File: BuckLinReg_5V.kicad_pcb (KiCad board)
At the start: 4 copper layers, 96 x 56 mm, 70 parts, among them J1 Barrel_Jack, J2 796638-4, J3 1x2 Male, Q1 PMBT2222, Q2 SQD40061EL, SW1 SW_SPDT, U1 TLV76050DBZT, U2 LMV358, U3 74HCT00, U4 SN74HCT02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

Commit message: PCB Ordered
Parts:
- removed TP14: ~Q, TestPoint:TestPoint_THTPad_D2.0mm_Drill1.0mm
- removed TP8: ~PWR_EN, TestPoint:TestPoint_THTPad_D2.0mm_Drill1.0mm
- Q2: value SQD40061EL -> Si4435FDY; footprint Package_TO_SOT_SMD:TO-252-2 -> Package_SO:SO-8_3.9x4.9mm_P1.27mm
- U7: value LM1084-5.0 -> LM1085ISX-5.0/NOPB
- moved C9 20.2 mm to (97.2, 73.0)
- moved C3 20.0 mm to (115.5, 64.5)
- moved TP3 8.86 mm to (72.0, 81.0)
- moved D1 8.50 mm to (79.5, 62.0)
- moved R1 7.63 mm to (85.5, 62.0)
- moved TP15 5.75 mm to (124.2, 103.2)
- moved TP13 5.30 mm to (124.2, 100.0)
- moved TP12 5.15 mm to (124.2, 106.5)
- moved Q2 4.79 mm to (80.0, 69.0)
- moved R14 3.51 mm to (112.5, 88.2), turned to 90 degrees
- moved J1 3.26 mm to (72.5, 71.2)
- moved TP10 3.01 mm to (97.7, 57.1)
- moved TP9 2.36 mm to (118.2, 104.2)
- moved TP1 2.32 mm to (90.2, 62.8)
- moved R13 2.26 mm to (109.8, 88.2), turned to 90 degrees
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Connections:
- C3 pad 1: /+Vin -> /SR+
- C9 pad 1: /SR+ -> /+Vin
- Q2 pad 1: /PCheckG -> /+Vin
- Q2 pad 2: /Vin -> /+Vin
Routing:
- net /~Q: track 36.3 -> 14.9 mm
- net /~PWR_EN: track 24.8 -> 13.9 mm, vias 1 -> 2
- net /+Vin: track 48.0 -> 38.1 mm
- net /SW: track 24.8 -> 15.1 mm
- net /PCheckG: track 10.00 -> 18.8 mm
- net /SR-: track 18.7 -> 25.5 mm
- net Net-(C7-Pad2): track 32.2 -> 25.8 mm
- net /Q: track 59.5 -> 53.3 mm
- net /DFA-: track 112.1 -> 106.2 mm
- net /OCP_TRIGGER: track 31.0 -> 25.2 mm, vias 1 -> 2
- net Net-(U4-Pad1): track 13.1 -> 8.54 mm, vias 2 -> 0
- net /S: track 5.48 -> 9.44 mm, vias 0 -> 2
- net /Vin: track 18.0 -> 14.3 mm
- net /Vo: track 26.2 -> 29.8 mm, vias 1 -> 3
- net /SR+: track 148.5 -> 146.1 mm
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- added copper zone on B.Cu, net /5V0_Out
- removed copper zone on In2.Cu, net GNDA
- removed copper zone on In1.Cu, net GNDPWR
- removed copper zone on In2.Cu, net GNDPWR
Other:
- copper layers 4 -> 2
- rule trace_min: 0.25 -> 0.15
- board text added: "+5V"
- board text added: "5V 2A MAX"
- board text added: "5V Converter Jack Sabine"
- board text added: "CHK POLAR"
- board text added: "GND"
- board text added: "JLCJLCJLCJLC"
- board text added: "OCP TRIG'D"
- board text added: "POWER IN +13 V MAX"
- board text added: "PWRD"

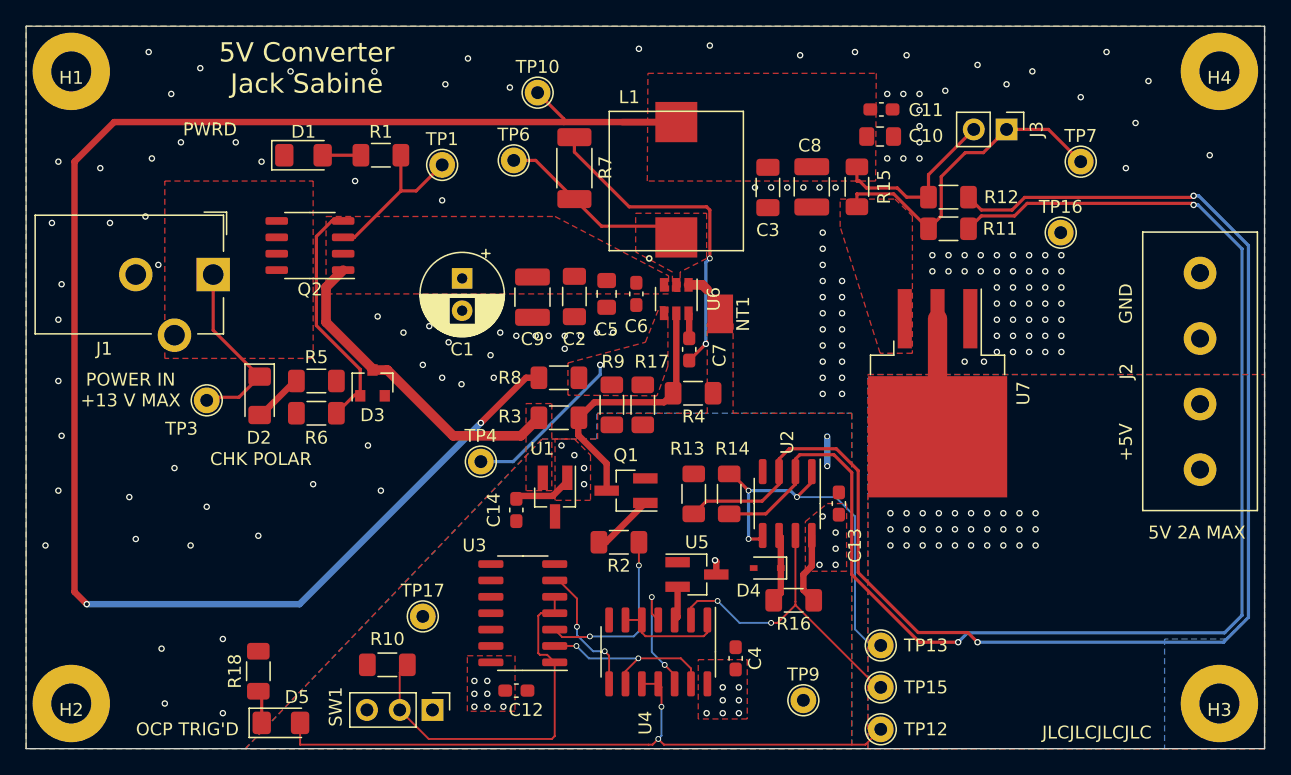
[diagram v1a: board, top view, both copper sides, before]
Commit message: Begin rev. 2 sch and PCB resize to 94x54mm
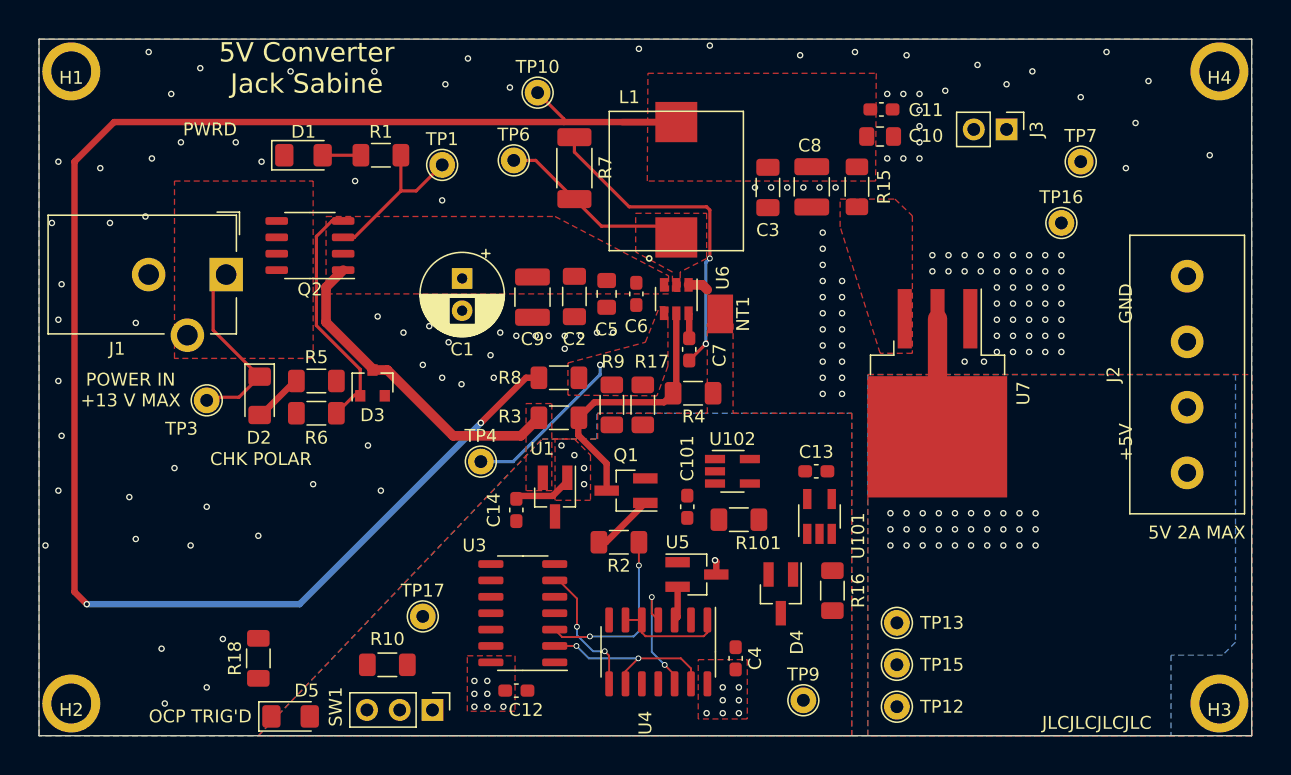
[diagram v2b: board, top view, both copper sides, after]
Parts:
- removed R11, R12: 1k, Resistor_SMD:R_1206_3216Metric_Pad1.30x1.75mm_HandSolder
- removed R13, R14: 100k, Resistor_SMD:R_1206_3216Metric_Pad1.30x1.75mm_HandSolder
- removed U2: LMV358, Package_SO:SOIC-8_3.9x4.9mm_P1.27mm
- added C101: 0.1u, Capacitor_SMD:C_0603_1608Metric_Pad1.08x0.95mm_HandSolder, F.Cu at (109.2, 89.2)
- added R101: 10k, Resistor_SMD:R_1206_3216Metric_Pad1.30x1.75mm_HandSolder, F.Cu at (113.2, 90.2)
- added U101: INA180A3IDBVR, Package_TO_SOT_SMD:SOT-23-5_HandSoldering, F.Cu at (119.5, 90.0)
- added U102: TLV7011KCKT, Package_TO_SOT_SMD:SOT-23-5_HandSoldering, F.Cu at (112.8, 86.5)
- D4: value 3.0 -> 2V4; footprint Diode_SMD:D_SOD-323 -> Package_TO_SOT_SMD:SOT-23_Handsoldering
- R16: value 10k -> 470
- moved R16 3.09 mm to (120.5, 95.8), turned to 90 degrees
- moved C13 3.05 mm to (119.2, 86.5), turned to 0 degrees
- moved D4 2.26 mm to (116.5, 96.0), turned to 270 degrees
- moved TP12 2.15 mm to (125.5, 104.8)
- moved TP13 2.15 mm to (125.5, 98.2)
- moved TP15 2.15 mm to (125.5, 101.5)
- moved J2 1.03 mm to (148.0, 79.0)
- moved J1 1.00 mm to (73.5, 71.2)
- moved R18 1.00 mm to (76.0, 101.0)
- moved D5 0.90 mm to (78.5, 105.5)
- moved TP16 0.75 mm to (138.2, 67.2)
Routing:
- net /DFA+: track 110.9 -> 0.00 mm, vias 2 -> 0
- net /DFA-: track 106.2 -> 0.00 mm, vias 2 -> 0
- net /Q: track 53.3 -> 0.00 mm, vias 2 -> 0
- net /Vo: track 29.8 -> 0.00 mm, vias 3 -> 0
- net /SW_SIG: track 29.6 -> 0.00 mm
- net /SR-: track 25.5 -> 0.00 mm
- net /OCP_TRIGGER: track 25.2 -> 0.00 mm, vias 2 -> 0
- net /SR+: track 146.1 -> 132.3 mm
- net /5V0_LOGIC: track 11.6 -> 5.93 mm, vias 24 -> 19
- net Net-(D4-Pad1): track 5.31 -> 0.00 mm
- net Net-(D5-Pad1): track 2.56 -> 0.00 mm
- net GNDA: track 2.30 -> 0.00 mm, vias 2 -> 0
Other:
- board size 96 x 56 mm -> 94 x 54 mm

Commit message: Completed initial layout of rev. 2
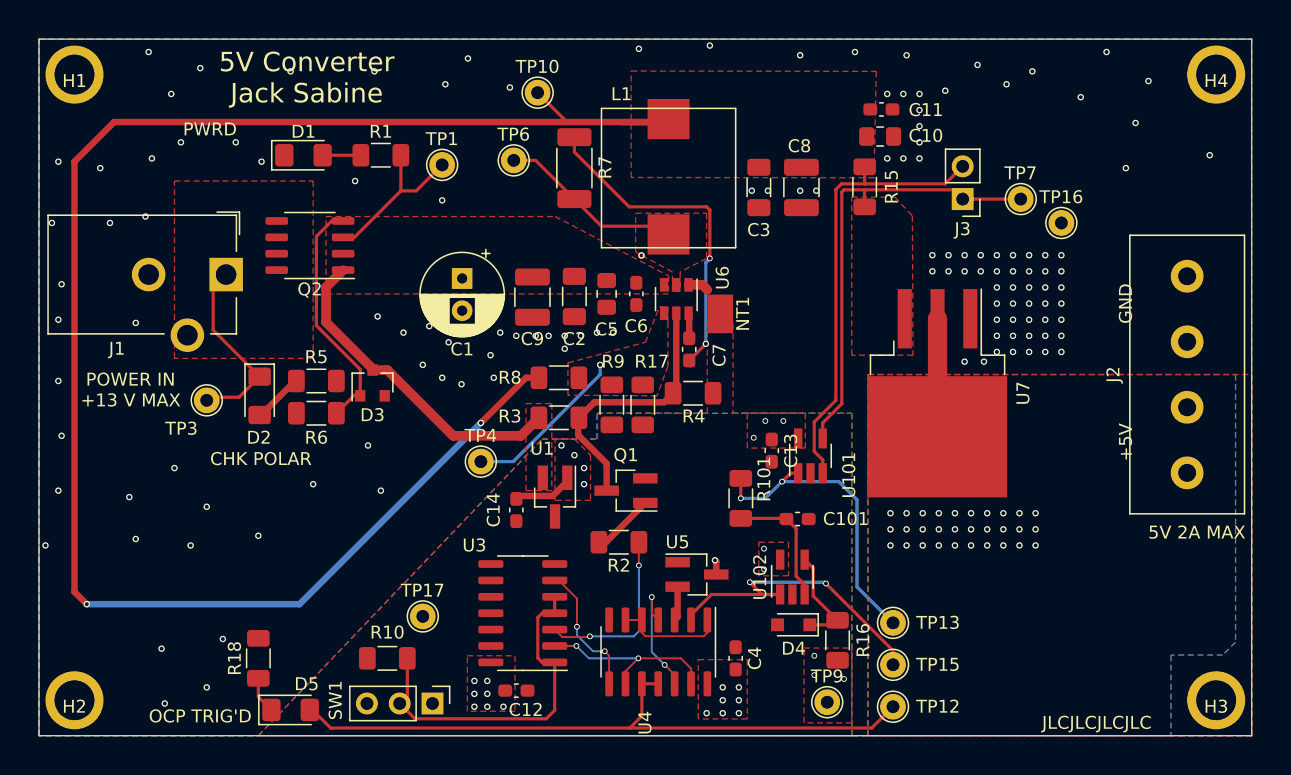
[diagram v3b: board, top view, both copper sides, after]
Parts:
- D4: footprint Package_TO_SOT_SMD:SOT-23_Handsoldering -> Diode_SMD:D_SOD-323_HandSoldering
- moved U102 9.43 mm to (117.4, 94.7), turned to 90 degrees
- moved C101 8.60 mm to (117.8, 90.2), turned to 0 degrees
- moved J3 6.38 mm to (130.6, 65.4), turned to 180 degrees
- moved TP7 5.48 mm to (135.1, 65.4)
- moved U101 4.75 mm to (118.8, 85.3)
- moved R16 3.87 mm to (120.9, 99.6)
- moved C13 3.80 mm to (115.8, 84.9), turned to 270 degrees
- moved D4 2.60 mm to (117.5, 98.4), turned to 180 degrees
- moved TP9 1.86 mm to (120.1, 104.4)
- moved R101 1.66 mm to (113.4, 88.6), turned to 270 degrees
- moved C8 0.80 mm to (118.1, 64.5)
- moved C3 0.70 mm to (114.8, 64.5)
- moved L1 0.64 mm to (107.8, 63.7)
- moved R15 0.60 mm to (123.0, 64.5)
- moved D5 0.50 mm to (78.5, 105.0)
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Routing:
- net /Q: track 0.00 -> 51.6 mm
- net /SR-: track 0.00 -> 35.3 mm
- net /SR+: track 132.3 -> 167.1 mm
- net /SW_SIG: track 0.00 -> 27.5 mm
- net /OCP_TRIGGER: track 0.00 -> 25.1 mm, vias 0 -> 2
- net /Vo: track 0.00 -> 23.9 mm, vias 0 -> 2
- net Net-(C101-Pad1): track 0.00 -> 9.99 mm
- net Net-(D4-Pad1): track 0.00 -> 8.05 mm
- net Net-(D5-Pad1): track 0.00 -> 2.87 mm
- net /5V0_LOGIC: vias 19 -> 27
- net GNDPWR: vias 151 -> 130

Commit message: Changed nettie and gnd clearances
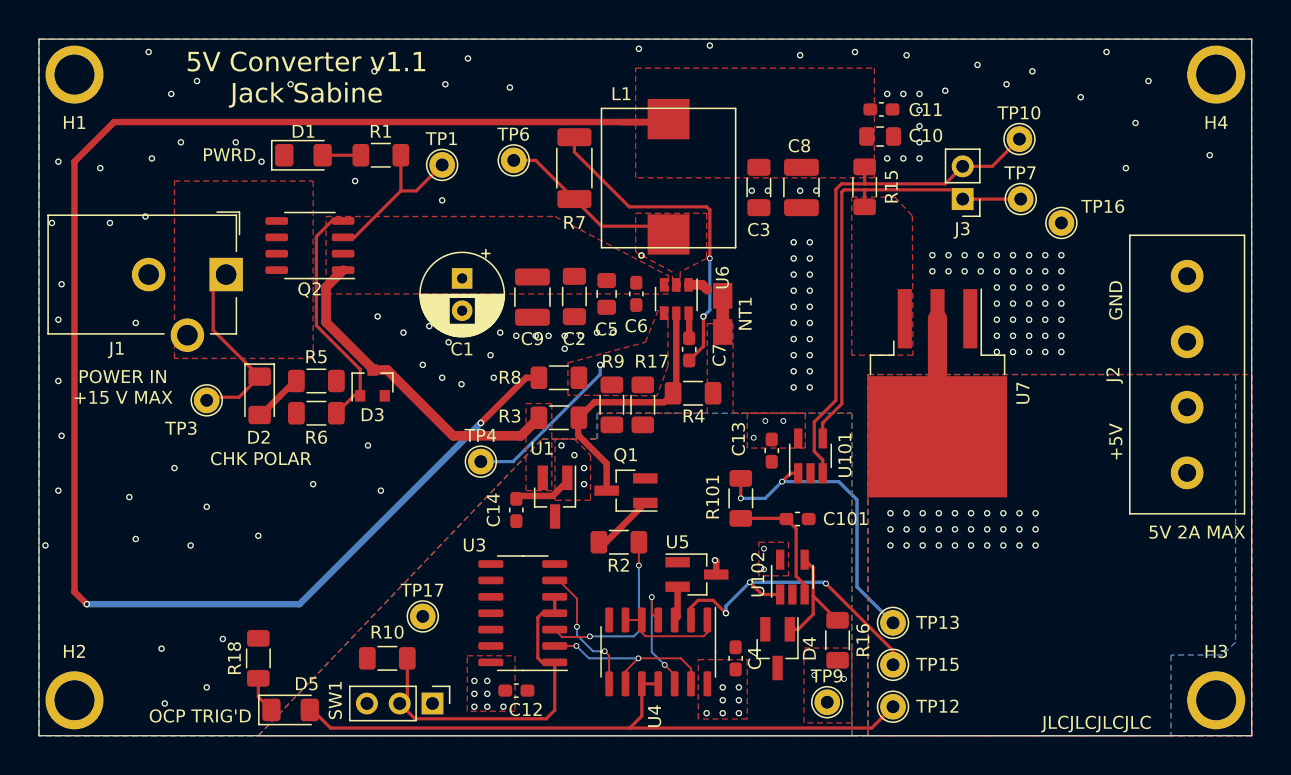
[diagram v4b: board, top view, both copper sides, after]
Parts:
- D4: footprint Diode_SMD:D_SOD-323_HandSoldering -> Package_TO_SOT_SMD:SOT-23_Handsoldering
- moved TP10 37.5 mm to (135.0, 60.8)
- moved D4 2.23 mm to (116.2, 100.2), turned to 270 degrees
- moved NT1 0.20 mm to (112.0, 74.3)
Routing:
- net /SR+: track 167.1 -> 169.3 mm
- net Net-(D4-Pad1): track 8.05 -> 9.97 mm
- net /OCP_TRIGGER: track 25.1 -> 24.6 mm, vias 2 -> 3
- net GNDPWR: vias 130 -> 148
- net /5V0_LOGIC: vias 27 -> 26
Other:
- board text added: "5V Converter v1.1 Jack Sabine"
- board text added: "POWER IN +15 V MAX"
- board text removed: "5V Converter Jack Sabine"
- board text removed: "POWER IN +13 V MAX"
